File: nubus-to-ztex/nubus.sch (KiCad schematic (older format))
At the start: 25 parts, among them J3 C96ABC, U1 74LVC1G07, U10 74FCT245ATQG, U11 74FCT245ATQG, U12 74FCT245ATQG, U8 XC9536XL-VQ44, U9 74FCT245ATQG

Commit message: large update
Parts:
- removed C4: 100nF, Capacitor_SMD:C_0603_1608Metric, symbol Device:C
- removed U1: 74LVC1G07, Package_TO_SOT_SMD:SOT-23-5, symbol 74xGxx:74LVC1G07
- added D1, D6, D7, D8: GREEN, LED_SMD:LED_0805_2012Metric, symbol Device:LED_ALT
- added D10, D11, D12, D13, D14, D15: YELLOW, LED_SMD:LED_0805_2012Metric, symbol Device:LED_ALT
- added D16, D17, D9: ORANGE, LED_SMD:LED_0805_2012Metric, symbol Device:LED_ALT
- added Q1, Q2: MMBT3904, Package_TO_SOT_SMD:SOT-23, symbol Transistor_BJT:MMBT3904
- added R21, R22, R27, R28, R29, R30, R31, R32, R33, R34, R35, R36, R37: 549, Resistor_SMD:R_0603_1608Metric, symbol Device:R
- added R38, R40: 1k, Resistor_SMD:R_0603_1608Metric, symbol Device:R
- added R39: 27, Resistor_SMD:R_0603_1608Metric, symbol Device:R
- C26: value 100nF -> 1uF; MPN CC0603KRX7R8BB104 -> CC0603KRX7R8BB105; Mouser 603-CC603KRX7R8BB104 -> 603-CC603KRX7R8BB105; URL (none) -> https://lcsc.com/product-detail/Multilayer-Ceramic-Capacito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
- R17: value 10k -> 27; MPN 0603WAF1002T5E -> 0603WAF270JT5E; MPN-ALT (none) -> ERJ-3EKF27R0V; URL (none) -> https://lcsc.com/product-detail/Chip-Resistor-Surface-Mount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
- U10, U11, U12: footprint Package_SO:QSOP-20_3.9x8.7mm_P0.635mm -> For_SeeedStudio:QSOP-20_3.9x8.7mm_P0.635mm_Renesas
- U8: MPN XC9536XL-10VQ44C -> XC9572XL-5VQ44C; NOTES (none) -> XC9536XL-*VQ44C (*=delay, 5/7/10) or XC9572XL-*VQ44C, they 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; URL https://www2.mouser.com/ProductDetail/?qs=rrS6PyfT74dzgfwyd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 -> https://www.mouser.fr/ProductDetail/Xilinx/XC9572XL-5VQ44C?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
- U9: footprint Package_SO:QSOP-20_3.9x8.7mm_P0.635mm -> For_SeeedStudio:QSOP-20_3.9x8.7mm_P0.635mm_Renesas; Datasheet - Packaging (none) -> https://www.renesas.com/document/psc/pcpcg-package-outline-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
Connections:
- net labels added: NMRQ, RQST_o
- net labels removed: VCC, fpga_to_cpld_signal_2, ~NMRQ_3V3
- wire segments 46 -> 74
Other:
- note added: "BEWARE: NMRQ from FPGA is active high!"
- note added: "BEWARE: RQST_o from CPLD is active high!"
- note added: "Internal signal tap leds"
- note added: "Signals Tap Leds"
- note added: "Slot ID Leds"
- note removed: "Open Collector Output\n(/nmrq)"
- note removed: "shuold be on B2B"

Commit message: another update after discussion on tinkerdifferent
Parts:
- removed Q1, Q2: MMBT3904, Package_TO_SOT_SMD:SOT-23, symbol Transistor_BJT:MMBT3904
- removed R17, R39: 27, Resistor_SMD:R_0603_1608Metric, symbol Device:R
- removed R38, R40: 1k, Resistor_SMD:R_0603_1608Metric, symbol Device:R
- removed U8: XC9536XL-VQ44, For_SeeedStudio:TQFP-44_10x10mm_P0.8mm_Xilinx, symbol xc9536xl-vq44:XC9536XL-VQ44
- added C33: 10nF, Capacitor_SMD:C_0603_1608Metric, symbol Device:C
- added C34, C35, C36: 100nF, Capacitor_SMD:C_0603_1608Metric, symbol Device:C
- added U1: XC9572XL-VQ64, For_SeeedStudio:TQFP-64_10x10mm_P0.5mm_Xlinx, symbol CPLD_Xilinx:XC9572XL-VQ64
- added U3, U8: 74LVC125, Package_SO:TSSOP-14_4.4x5mm_P0.65mm, symbol 74xx:74LVC125
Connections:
- net +3V3: now also C33.1, C34.1, C35.1, C36.1, U1.26 (VCCIO), U1.3 (VCC), U1.37 (VCC), U1.55 (VCCIO), U3.14 (VCC), U8.1, U8.14 (VCC), U8.4
- net ARB: now also U1.56 (P56)
- net CPLD_JTAG_TCK: now also U1.30 (TCK)
- net CPLD_JTAG_TDI: now also U1.28 (TDI)
- net CPLD_JTAG_TDO: now also U1.53 (TDO)
- net CPLD_JTAG_TMS: now also U1.29 (TMS)
- net GND: now also C33.2, C34.2, C35.2, C36.2, U1.14 (GND), U1.21 (GND), U1.41 (GND), U1.54 (GND), U3.12, U3.2, U3.5, U3.7 (GND), U3.9, U8.12, U8.2, U8.5, U8.7 (GND), U8.9
- net GRANT: now also U1.57 (P57)
- net NUBUS_MASTER_DIR: now also U1.49 (P49)
- net NUBUS_OE: now also U1.46 (P46)
- net fpga_to_cpld_clk: now also U1.15 (I/O/GCK1)
- net fpga_to_cpld_signal: now also U1.6 (P6)
- net tmoen: now also U1.51 (P51)
- net ~ACK_3V3: now also U1.5 (I/O/GTS1)
- net ~ACK_5V: now also U1.11 (P11)
- net ~ARB0_5V: now also U1.34 (P34), U3.3
- net ~ARB1_5V: now also U1.36 (P36), U3.6
- net ~ARB2_5V: now also U1.27 (P27), U3.11
- net ~ARB3_5V: now also U1.32 (P32), U3.8
- net ~CLK2X_5V: now also U1.17 (I/O/GCK3)
- net ~CLK_3V3: now also U1.47 (P47)
- net ~CLK_5V: now also U1.16 (I/O/GCK2)
- net ~ID0_3V3: now also U1.61 (P61)
- net ~ID0_5V: now also U1.20 (P20)
- net ~ID1_3V3: now also U1.62 (P62)
- net ~ID1_5V: now also U1.19 (P19)
- net ~ID2_3V3: now also U1.63 (P63)
- net ~ID2_5V: now also U1.18 (P18)
- net ~ID3_3V3: now also U1.64 (I/O/GSR)
- net ~ID3_5V: now also U1.8 (P8)
- net ~NMRQ_5V: now also U8.8
- net ~RESET_3V3: now also U1.48 (P48)
- net ~RESET_5V: now also U1.45 (P45)
- net ~RQST_3V3: now also U1.4 (P4)
- net ~RQST_5V: now also U1.10 (P10), U8.11
- net ~START_3V3: now also U1.7 (P7)
- net ~START_5V: now also U1.12 (P12)
- net ~TM0_3V3: now also U1.2 (I/O/GTS2)
- net ~TM0_5V: now also U1.44 (P44)
- net ~TM1_3V3: now also U1.1 (P1)
- net ~TM1_5V: now also U1.43 (P43)
- net ~TM2_5V: now also U1.22 (P22)
- new net ARB0_o_n: U1.33 (P33), U3.1
- new net ARB1_o_n: U1.35 (P35), U3.4
- new net ARB2_o_n: U1.25 (P25), U3.13
- new net ARB3_o_n: U1.31 (P31), U3.10
- new net RQST_o_n: U1.9 (P9), U8.13
- new net fpga_to_cpld_signal_2: U1.50 (P50)
- new net ~CLK2X_3V3: U1.60 (P60)
- new net ~NMRQ_3V3: U8.10
- new net ~TM2_3V3: U1.59 (P59)
- no-connect marks 13 -> 15
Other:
- note removed: "BEWARE: NMRQ from FPGA is active high!"
- note removed: "BEWARE: RQST_o from CPLD is active high!"
- moved on the sheet: C1, C22, C26, C27, C28, C3, C30, R23, R24, R25, R26

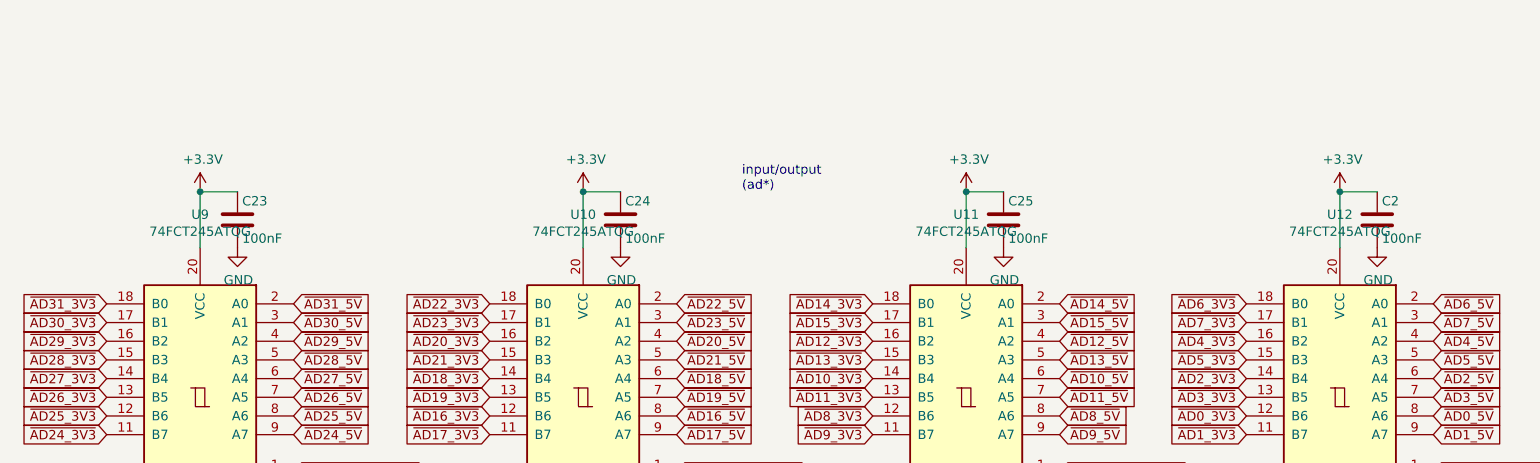
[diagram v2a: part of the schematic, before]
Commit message: Switch from 5V 74FCT245 to 3.3V 74LVT245
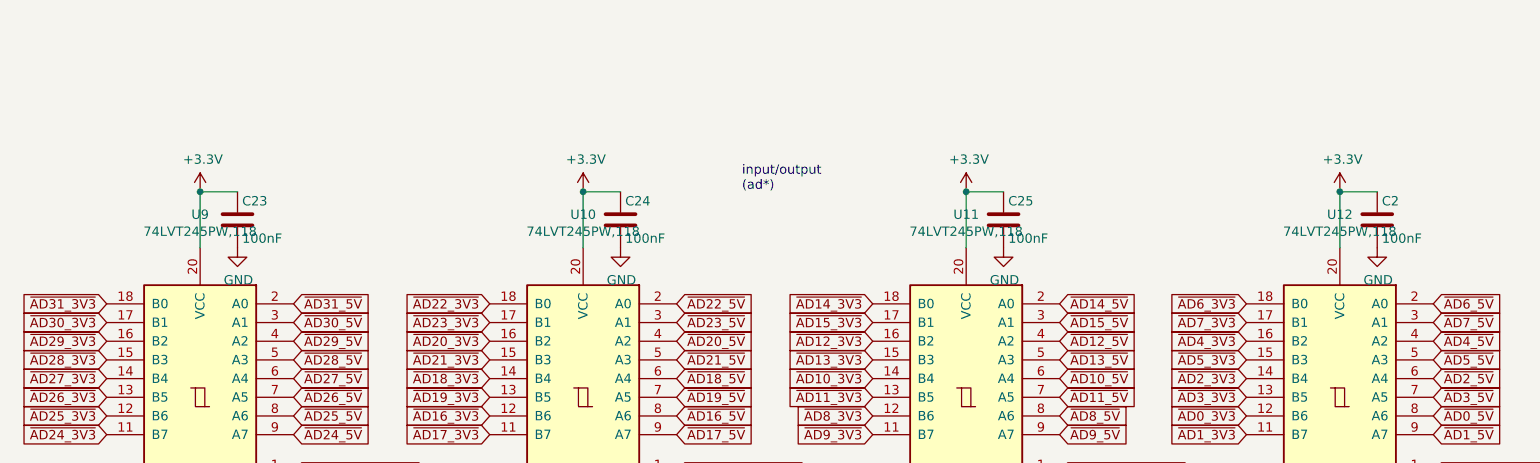
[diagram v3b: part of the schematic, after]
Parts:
- U10, U11, U12, U9: value 74FCT245ATQG -> 74LVT245PW,118; footprint For_SeeedStudio:QSOP-20_3.9x8.7mm_P0.635mm_Renesas -> For_SeeedStudio:TSSOP-20_4.4x6.5mm_P0.65mm_ForSeeedStudio; MPN 74FCT245ATQG -> 74LVT245PW,118; URL https://www.mouser.fr/ProductDetail/Renesas-IDT/74FCT245ATQ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 -> https://eu.mouser.com/ProductDetail/Nexperia/74LVT245PW118?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
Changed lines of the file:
@@
 P 17350 3450
 F 0 "U12" H 17350 4428 50  0000 C CNN
-F 1 "74FCT245ATQG" H 17350 4337 50  0000 C CNN
-F 2 "For_SeeedStudio:QSOP-20_3.9x8.7mm_P0.635mm_Renesas" H 17350 3450 50  0001 C CNN
+F 1 "74LVT245PW,118" H 17350 4337 50  0000 C CNN
+F 2 "For_SeeedStudio:TSSOP-20_4.4x6.5mm_P0.65mm_ForSeeedStudio" H 17350 3450 50  0001 C CNN
 F 3 "http://www.ti.com/lit/gpn/sn74LS245" H 17350 3450 50  0001 C CNN
-F 4 "https://www.mouser.fr/ProductDetail/Renesas-IDT/74FCT245ATQG?qs=JcGQCygHkIZJMVzrAcertA%3D%3D" H 17350 3450 50  0001 C CNN "URL"
-F 5 "74FCT245ATQG" H 17350 3450 50  0001 C CNN "MPN"
+F 4 "https://eu.mouser.com/ProductDetail/Nexperia/74LVT245PW118?qs=me8TqzrmIYWNf3DjNNs5mQ%3D%3D" H 17350 3450 50  0001 C CNN "URL"
+F 5 "74LVT245PW,118" H 17350 3450 50  0001 C CNN "MPN"
 	1    17350 3450
 	-1   0    0    -1
@@
 P 15350 3450
 F 0 "U11" H 15350 4428 50  0000 C CNN
-F 1 "74FCT245ATQG" H 15350 4337 50  0000 C CNN
-F 2 "For_SeeedStudio:QSOP-20_3.9x8.7mm_P0.635mm_Renesas" H 15350 3450 50  0001 C CNN
+F 1 "74LVT245PW,118" H 15350 4337 50  0000 C CNN
+F 2 "For_SeeedStudio:TSSOP-20_4.4x6.5mm_P0.65mm_ForSeeedStudio" H 15350 3450 50  0001 C CNN
 F 3 "http://www.ti.com/lit/gpn/sn74LS245" H 15350 3450 50  0001 C CNN
-F 4 "74FCT245ATQG" H 15350 3450 50  0001 C CNN "MPN"
-F 5 "https://www.mouser.fr/ProductDetail/Renesas-IDT/74FCT245ATQG?qs=JcGQCygHkIZJMVzrAcertA%3D%3D" H 15350 3450 50  0001 C CNN "URL"
+F 4 "74LVT245PW,118" H 15350 3450 50  0001 C CNN "MPN"
+F 5 "https://eu.mouser.com/ProductDetail/Nexperia/74LVT245PW118?qs=me8TqzrmIYWNf3DjNNs5mQ%3D%3D" H 15350 3450 50  0001 C CNN "URL"
 	1    15350 3450
 	-1   0    0    -1
@@
 P 13300 3450
 F 0 "U10" H 13300 4428 50  0000 C CNN
-F 1 "74FCT245ATQG" H 13300 4337 50  0000 C CNN
-F 2 "For_SeeedStudio:QSOP-20_3.9x8.7mm_P0.635mm_Renesas" H 13300 3450 50  0001 C CNN
+F 1 "74LVT245PW,118" H 13300 4337 50  0000 C CNN
+F 2 "For_SeeedStudio:TSSOP-20_4.4x6.5mm_P0.65mm_ForSeeedStudio" H 13300 3450 50  0001 C CNN
 F 3 "http://www.ti.com/lit/gpn/sn74LS245" H 13300 3450 50  0001 C CNN
-F 4 "74FCT245ATQG" H 13300 3450 50  0001 C CNN "MPN"
-F 5 "https://www.mouser.fr/ProductDetail/Renesas-IDT/74FCT245ATQG?qs=JcGQCygHkIZJMVzrAcertA%3D%3D" H 13300 3450 50  0001 C CNN "URL"
+F 4 "74LVT245PW,118" H 13300 3450 50  0001 C CNN "MPN"
+F 5 "https://eu.mouser.com/ProductDetail/Nexperia/74LVT245PW118?qs=me8TqzrmIYWNf3DjNNs5mQ%3D%3D" H 13300 3450 50  0001 C CNN "URL"
 	1    13300 3450
 	-1   0    0    -1
@@
 P 11250 3450
 F 0 "U9" H 11250 4428 50  0000 C CNN
-F 1 "74FCT245ATQG" H 11250 4337 50  0000 C CNN
-F 2 "For_SeeedStudio:QSOP-20_3.9x8.7mm_P0.635mm_Renesas" H 11250 3450 50  0001 C CNN
+F 1 "74LVT245PW,118" H 11250 4337 50  0000 C CNN
+F 2 "For_SeeedStudio:TSSOP-20_4.4x6.5mm_P0.65mm_ForSeeedStudio" H 11250 3450 50  0001 C CNN
 F 3 "http://www.ti.com/lit/gpn/sn74LS245" H 11250 3450 50  0001 C CNN
-F 4 "74FCT245ATQG" H 11250 3450 50  0001 C CNN "MPN"
-F 5 "https://www.mouser.fr/ProductDetail/Renesas-IDT/74FCT245ATQG?qs=JcGQCygHkIZJMVzrAcertA%3D%3D" H 11250 3450 50  0001 C CNN "URL"
+F 4 "74LVT245PW,118" H 11250 3450 50  0001 C CNN "MPN"
+F 5 "https://eu.mouser.com/ProductDetail/Nexperia/74LVT245PW118?qs=me8TqzrmIYWNf3DjNNs5mQ%3D%3D" H 11250 3450 50  0001 C CNN "URL"
 F 6 "https://www.renesas.com/us/en/package/pcg20" H 11250 3450 50  0001 C CNN "Drawings"
 F 7 "https://www.renesas.com/document/psc/pcpcg-package-outline-150-body-width-qsop-025-pitch?language=en" H 11250 3450 50  0001 C CNN "Datasheet - Packaging"

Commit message: large clean-up update
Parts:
- removed D9: ORANGE, LED_SMD:LED_0805_2012Metric, symbol Device:LED_ALT
- removed R29: 549, Resistor_SMD:R_0603_1608Metric, symbol Device:R
- added C5: 100nF, Capacitor_SMD:C_0603_1608Metric, symbol Device:C
- added D10: YELLOW, LED_SMD:LED_0805_2012Metric, symbol Device:LED_ALT
- added R15: 549, Resistor_SMD:R_0603_1608Metric, symbol Device:R
- added U2: 74LVT125, Package_SO:TSSOP-14_4.4x5mm_P0.65mm, symbol 74xx:74LVC125
- J4: renamed from J3; MPN (3M) (none) -> DIN-096CPC-RR1-HM; MPN (Harting 2) (none) -> 09033966921; MPN (Harting) (none) -> 09033967921; MPN - no fixing clip 85003-0177 -> (none); Notes (3M) (none) -> RR1L would also work (for .062 PCBs); URL- no fixing clip https://www2.mouser.com/ProductDetail/Molex/85003-0177?qs=U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 -> (none)
- U1: renamed from U8; value 74LVC125 -> 74LVT125; MPN 74LVT125PW -> 74LVT125PW,118; URL (none) -> https://eu.mouser.com/ProductDetail/Nexperia/74LVT125PW118?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
- U1: renamed from U8; value 74LVC125 -> 74LVT125; footprint (none) -> Package_SO:TSSOP-14_4.4x5mm_P0.65mm; MPN (none) -> 74LVT125PW,118
- U3: value 74LVC125 -> 74LVT125; MPN 74LVT125PW -> 74LVT125PW,118; URL (none) -> https://eu.mouser.com/ProductDetail/Nexperia/74LVT125PW118?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
- U3: value 74LVC125 -> 74LVT125; footprint (none) -> Package_SO:TSSOP-14_4.4x5mm_P0.65mm; MPN (none) -> 74LVT125PW,118
- U5: renamed from U9; value 74LVT245PW,118 -> 74LVT245BPW,118; MPN 74LVT245PW,118 -> 74LVT245BPW,118; Package Drawings (none) -> https://assets.nexperia.com/documents/package-information/S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; URL https://eu.mouser.com/ProductDetail/Nexperia/74LVT245PW118?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 -> https://eu.mouser.com/ProductDetail/?qs=me8TqzrmIYVnC5%252B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
- U6: renamed from U10; value 74LVT245PW,118 -> 74LVT245BPW,118; MPN 74LVT245PW,118 -> 74LVT245BPW,118; URL https://eu.mouser.com/ProductDetail/Nexperia/74LVT245PW118?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 -> https://eu.mouser.com/ProductDetail/?qs=me8TqzrmIYVnC5%252B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
- U7: renamed from U11; value 74LVT245PW,118 -> 74LVT245BPW,118; MPN 74LVT245PW,118 -> 74LVT245BPW,118; URL https://eu.mouser.com/ProductDetail/Nexperia/74LVT245PW118?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 -> https://eu.mouser.com/ProductDetail/?qs=me8TqzrmIYVnC5%252B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
- U8: renamed from U12; value 74LVT245PW,118 -> 74LVT245BPW,118; MPN 74LVT245PW,118 -> 74LVT245BPW,118; URL https://eu.mouser.com/ProductDetail/Nexperia/74LVT245PW118?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 -> https://eu.mouser.com/ProductDetail/?qs=me8TqzrmIYVnC5%252B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
- renumbered C27 to C10, C28 to C11, C30 to C12, C26 to C13, C23 to C14, C33 to C15, C34 to C16, C24 to C17, C25 to C18, C2 to C19, C36 to C4, C35 to C6, C3 to C7, C22 to C8, C1 to C9, D1 to D11, D6 to D12, D7 to D13, D8 to D14, D14 to D15, D15 to D16, D16 to D4, D17 to D5, D10 to D6, D11 to D7, D12 to D8, D13 to D9, R37 to R10, R30 to R11, R31 to R12, R32 to R13, R33 to R14, R21 to R16, R22 to R17, R27 to R18, R28 to R19, R34 to R20, R35 to R21, R13 to R4, R23 to R5, R24 to R6, R25 to R7, R26 to R8, R36 to R9, U1 to U4
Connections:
- net +3V3: now also C5.1, R15.1, U2.13, U2.14 (VCC); no longer U1.1, U1.4
- net +5V: now also R8.2; no longer R8.1
- net ARB: now also U4.52 (P52); no longer U4.56 (P56)
- net GND: now also C5.2, U2.12, U2.7 (GND); no longer U1.12, U1.9
- net GRANT: now also U4.56 (P56); no longer U4.57 (P57)
- net NUBUS_OE: now also U4.45 (P45); no longer U4.46 (P46)
- net RQST_o_n: now also U1.4, U4.5 (I/O/GTS1); no longer U1.13, U4.9 (P9)
- net fpga_to_cpld_signal: now also U4.23 (P23); no longer U4.6 (P6)
- net ~ACK_3V3: now also U4.2 (I/O/GTS2); no longer U4.5 (I/O/GTS1)
- net ~ACK_5V: now also U1.11, U4.10 (P10); no longer U4.11 (P11)
- net ~CLK2X_3V3: now also U4.58 (P58); no longer U4.60 (P60)
- net ~ID0_3V3: now also U4.59 (P59); no longer U4.61 (P61)
- net ~ID1_3V3: now also U4.60 (P60); no longer U4.62 (P62)
- net ~ID3_3V3: now also U4.1 (P1); no longer U4.64 (I/O/GSR)
- net ~ID3_5V: now also R8.1, U4.7 (P7); no longer R8.2, U4.8 (P8)
- net ~NMRQ_3V3: now also U1.1; no longer U1.10
- net ~NMRQ_5V: now also U1.3; no longer U1.8
- net ~RESET_3V3: now also D10.1 (K)
- net ~RESET_5V: now also U4.44 (P44); no longer U4.45 (P45)
- net ~RQST_3V3: now also U4.64 (I/O/GSR); no longer U4.4 (P4)
- net ~RQST_5V: now also U1.6, U4.6 (P6); no longer U1.11, U4.10 (P10)
- net ~START_3V3: now also U4.4 (P4); no longer U4.7 (P7)
- net ~START_5V: now also U1.8, U4.13 (P13); no longer U4.12 (P12)
- net ~TM0_3V3: now also U4.61 (P61); no longer U4.2 (I/O/GTS2)
- net ~TM0_5V: now also U4.39 (P39), U2.6; no longer U4.44 (P44)
- net ~TM1_3V3: now also U4.62 (P62); no longer U4.1 (P1)
- net ~TM1_5V: now also U4.38 (P38), U2.3; no longer U4.43 (P43)
- net ~TM2_3V3: now also U4.57 (P57); no longer U4.59 (P59)
- net ~TM2_5V: now also U2.8
- net TM2_oe_n: now reaches U4.24 (P24)
- net TM2_oe_n: now also U2.10
- net TM1_n_o: now reaches U4.40 (P40)
- net TM1_n_o: now also U2.2
- net TM0_n_o: now reaches U4.42 (P42)
- net TM0_n_o: now also U2.5
- new net: D10.2 (A), R15.2
- new net ACK_o_n: U1.12, U4.9 (P9)
- new net ACK_oe_n: U1.13, U4.8 (P8)
- new net START_o_n: U1.9, U4.12 (P12)
- new net START_oe_n: U1.10, U4.11 (P11)
- new net TM2_o_n: U2.9, U4.46 (P46)
- new net TMx_oe_n: U2.1, U2.4, U4.43 (P43)
- no-connect marks 15 -> 12
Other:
- note added: "74LVT125 used for 'open collector'\n'Input' is tied low\n'/OE' is used as input\n'/OE' low -> enable -> output is low\n'/OE' high -> disable -> ouput is Z"
- note added: "DIN header for NuBus\n3x32 pins"
- note added: "Non-connected\nNuBus signals"
- note added: "Normal tri-state use\n_5V: output to NuBus (all are active low)\n_o_n: output value (active low)\n_oe_n: output enable (active low)"
- note added: "Open Collector"
- note added: "Slot ID Leds\n(pull-ups are on the 5V side of the CPLD)"
- note added: "disabled"
- note added: "input/output\n(ad*)\n74LVT245 with enable (always on except after reset) and direction pin"
- note removed: "NuBus 90 2x transfers\n(unused)"
- note removed: "Slot ID Leds"
- note removed: "input/output\n(ad*)\n"
- moved on the sheet: C4, C6, U1E, U3E

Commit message: more updates
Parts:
- added R36, R37, R38, R39, R40, R41, R42, R43, R44, R45: 10k, Resistor_SMD:R_0603_1608Metric, symbol Device:R
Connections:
- net +3V3: now also R36.1, R37.1, R38.1, R39.1, R40.1, R41.1, R42.1, R43.1, R44.1, R45.1
- net ACK_oe_n: now also R39.2
- net ARB0_o_n: now also R42.2
- net ARB1_o_n: now also R43.2
- net ARB2_o_n: now also R44.2
- net ARB3_o_n: now also R45.2
- net RQST_o_n: now also R37.2
- net START_oe_n: now also R38.2
- net TM2_oe_n: now also R41.2
- net TMx_oe_n: now also R40.2
- net ~NMRQ_3V3: now also R36.2
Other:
- note added: "Pull-ups on OE signals for drivers"
- note removed: "NUBUS_OE pullup"
- moved on the sheet: R4

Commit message: some missing stuff, minor HW update, SW
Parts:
- U5, U6, U7, U8: URL https://eu.mouser.com/ProductDetail/?qs=me8TqzrmIYVnC5%252B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 -> https://www.digikey.fr/fr/products/detail/nexperia-usa-inc/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; URL-mouser (none) -> https://eu.mouser.com/ProductDetail/?qs=me8TqzrmIYVnC5%252B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
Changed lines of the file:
@@
 F 2 "For_SeeedStudio:TSSOP-20_4.4x6.5mm_P0.65mm_ForSeeedStudio" H 17350 3450 50  0001 C CNN
 F 3 "http://www.ti.com/lit/gpn/sn74LS245" H 17350 3450 50  0001 C CNN
-F 4 "https://eu.mouser.com/ProductDetail/?qs=me8TqzrmIYVnC5%252BK4SaiTg%3D%3D" H 17350 3450 50  0001 C CNN "URL"
+F 4 "https://eu.mouser.com/ProductDetail/?qs=me8TqzrmIYVnC5%252BK4SaiTg%3D%3D" H 17350 3450 50  0001 C CNN "URL-mouser"
 F 5 "74LVT245BPW,118" H 17350 3450 50  0001 C CNN "MPN"
+F 6 "https://www.digikey.fr/fr/products/detail/nexperia-usa-inc/74LVT245BPW-118/1231957" H 17350 3450 50  0001 C CNN "URL"
 	1    17350 3450
 	-1   0    0    -1
@@
 F 3 "http://www.ti.com/lit/gpn/sn74LS245" H 15350 3450 50  0001 C CNN
 F 4 "74LVT245BPW,118" H 15350 3450 50  0001 C CNN "MPN"
-F 5 "https://eu.mouser.com/ProductDetail/?qs=me8TqzrmIYVnC5%252BK4SaiTg%3D%3D" H 15350 3450 50  0001 C CNN "URL"
+F 5 "https://eu.mouser.com/ProductDetail/?qs=me8TqzrmIYVnC5%252BK4SaiTg%3D%3D" H 15350 3450 50  0001 C CNN "URL-mouser"
+F 6 "https://www.digikey.fr/fr/products/detail/nexperia-usa-inc/74LVT245BPW-118/1231957" H 15350 3450 50  0001 C CNN "URL"
 	1    15350 3450
 	-1   0    0    -1
@@
 F 3 "http://www.ti.com/lit/gpn/sn74LS245" H 13300 3450 50  0001 C CNN
 F 4 "74LVT245BPW,118" H 13300 3450 50  0001 C CNN "MPN"
-F 5 "https://eu.mouser.com/ProductDetail/?qs=me8TqzrmIYVnC5%252BK4SaiTg%3D%3D" H 13300 3450 50  0001 C CNN "URL"
+F 5 "https://eu.mouser.com/ProductDetail/?qs=me8TqzrmIYVnC5%252BK4SaiTg%3D%3D" H 13300 3450 50  0001 C CNN "URL-mouser"
+F 6 "https://www.digikey.fr/fr/products/detail/nexperia-usa-inc/74LVT245BPW-118/1231957" H 13300 3450 50  0001 C CNN "URL"
 	1    13300 3450
 	-1   0    0    -1
@@
 F 3 "http://www.ti.com/lit/gpn/sn74LS245" H 11250 3450 50  0001 C CNN
 F 4 "74LVT245BPW,118" H 11250 3450 50  0001 C CNN "MPN"
-F 5 "https://eu.mouser.com/ProductDetail/?qs=me8TqzrmIYVnC5%252BK4SaiTg%3D%3D" H 11250 3450 50  0001 C CNN "URL"
+F 5 "https://eu.mouser.com/ProductDetail/?qs=me8TqzrmIYVnC5%252BK4SaiTg%3D%3D" H 11250 3450 50  0001 C CNN "URL-mouser"
 F 6 "https://www.renesas.com/us/en/package/pcg20" H 11250 3450 50  0001 C CNN "Drawings"
 F 7 "https://www.renesas.com/document/psc/pcpcg-package-outline-150-body-width-qsop-025-pitch?language=en" H 11250 3450 50  0001 C CNN "Datasheet - Packaging"
 F 8 "https://assets.nexperia.com/documents/package-information/SOT360-1.pdf" H 11250 3450 50  0001 C CNN "Package Drawings"
+F 9 "https://www.digikey.fr/fr/products/detail/nexperia-usa-inc/74LVT245BPW-118/1231957" H 11250 3450 50  0001 C CNN "URL"
 	1    11250 3450
 	-1   0    0    -1
